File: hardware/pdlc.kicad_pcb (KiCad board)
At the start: 2 copper layers, 56 x 36 mm, 57 parts, among them J1 TBP01R1-508-06BE, Q1 S8550, U1 LM5158, U2 DRV8262DDWR, U3 TLC555IDR

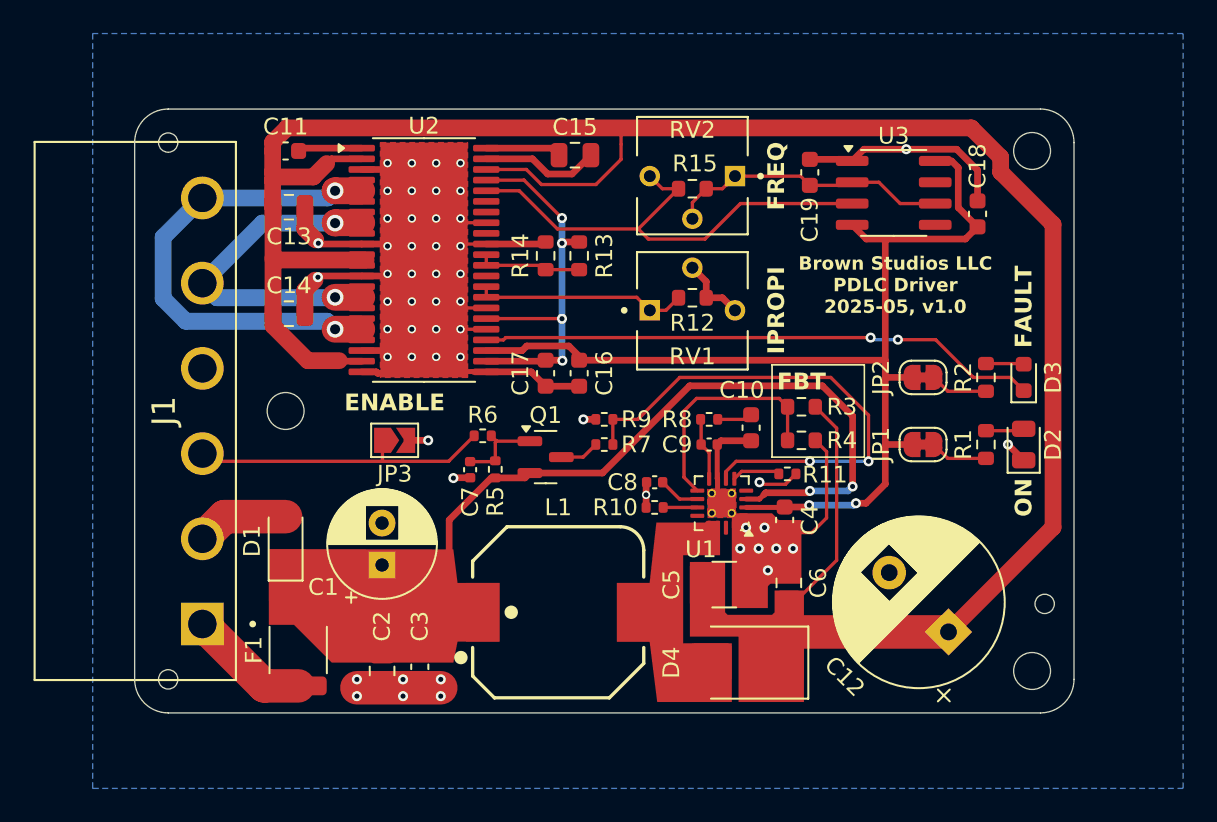
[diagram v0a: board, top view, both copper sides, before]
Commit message: Revised layout using LM5108 and discrete FETs
LM5108 is less expensive but it requires more board area.  In lieu of
active current limiting, we rely on the LM5158 hiccup overload
protection.  The FETs are intentionally oversized to handle large
current pulses when switching the polarity of the capacitive load.

This design is complete and ready for manufacture.
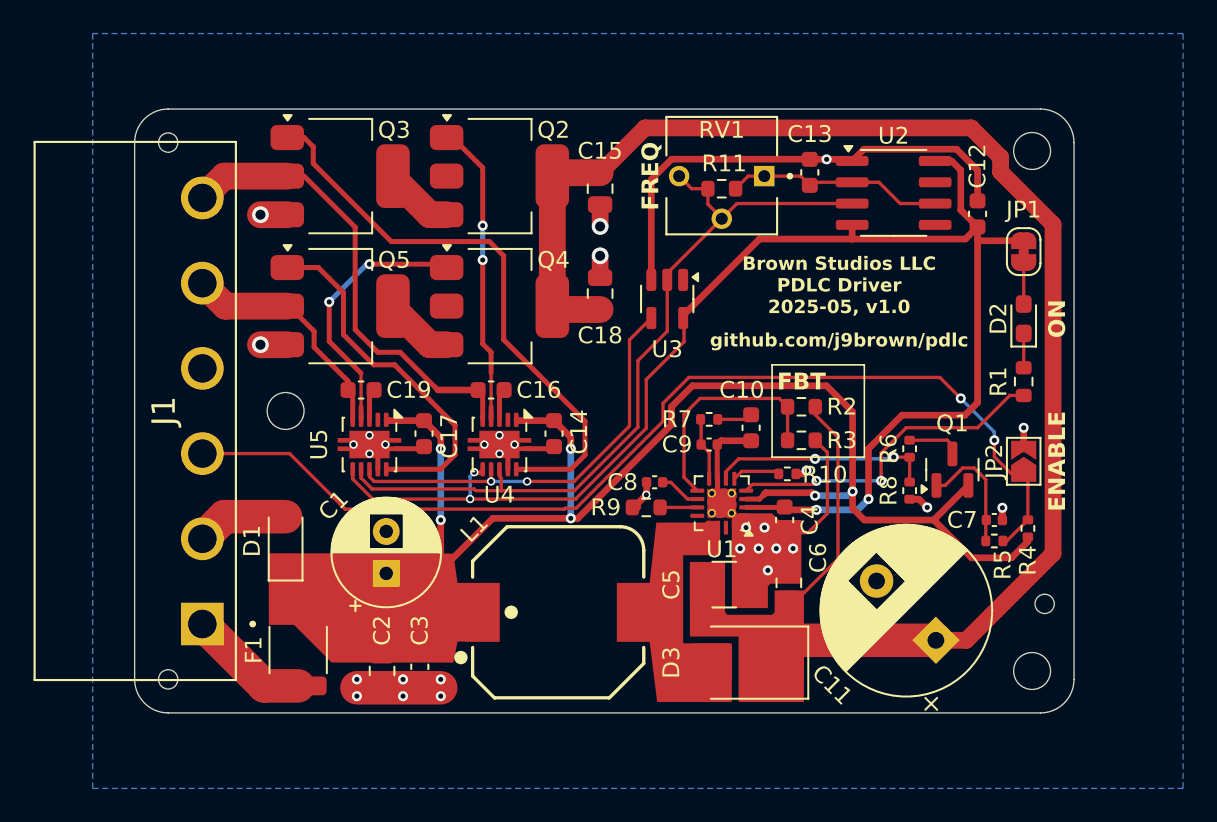
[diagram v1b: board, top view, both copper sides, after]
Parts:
- removed the C12 at (128.5, 113.2)
- removed the C13 at (89.2, 87.8)
- removed the D3 at (133.0, 98.0)
- removed the JP2 at (127.0, 98.0)
- removed R12: 4.7K, Resistor_SMD:R_0603_1608Metric
- removed R13, R14: 100K, Resistor_SMD:R_0603_1608Metric
- removed the R2 at (130.8, 98.0)
- removed the RV1 at (113.2, 94.0)
- removed the U2 at (97.2, 91.0)
- added C18: 100n, Capacitor_SMD:C_0805_2012Metric, F.Cu at (107.8, 93.0)
- added C19: 1u, Capacitor_SMD:C_0603_1608Metric, F.Cu at (93.5, 98.8)
- added Q2: DMN10H120SE, Package_TO_SOT_SMD:SOT-223, F.Cu at (101.8, 86.0)
- added Q3: DMN10H120SE, Package_TO_SOT_SMD:SOT-223, F.Cu at (92.2, 86.0)
- added Q4: DMN10H120SE, Package_TO_SOT_SMD:SOT-223, F.Cu at (101.8, 93.8)
- added Q5: DMN10H120SE, Package_TO_SOT_SMD:SOT-223, F.Cu at (92.2, 93.8)
- added U3: SN74LVC1G14DBV, Package_TO_SOT_SMD:SOT-23-5, F.Cu at (111.8, 93.3)
- added U4: LM5108DRC, Package_SON:VSON-10-1EP_3x3mm_P0.5mm_EP1.65x2.4mm, F.Cu at (101.8, 102.0)
- added U5: LM5108DRC, Package_SON:VSON-10-1EP_3x3mm_P0.5mm_EP1.65x2.4mm, F.Cu at (94.0, 102.0)
- C11: value 1u -> 100u; footprint Capacitor_SMD:C_0603_1608Metric -> Capacitor_THT:CP_Radial_D10.0mm_P5.00mm
- C14: value 100n -> 10u; footprint Capacitor_SMD:C_0805_2012Metric -> Capacitor_SMD:C_0603_1608Metric
- C16: value 100n -> 1u
- C17: value 1u -> 10u
- D2: value KT-0805G -> KT-0603R; footprint LED_SMD:LED_0805_2012Metric -> LED_SMD:LED_0603_1608Metric_Pad1.05x0.95mm_HandSolder
- F1: footprint Fuse:Fuse_1812_4532Metric -> 1812L:1812L
- R5: renamed from R6; value 100K -> 20K
- R9: renamed from R10; value 100K -> 39K; footprint Resistor_SMD:R_0402_1005Metric -> Resistor_SMD:R_0603_1608Metric
- moved C11 48.5 mm to (127.8, 113.7), turned to 135 degrees
- moved JP2 37.5 mm to (133.0, 103.0), turned to 90 degrees
- moved R4 31.9 mm to (133.2, 107.0)
- moved C7 31.4 mm to (131.2, 106.5), turned to 0 degrees
- moved R5 31.1 mm to (131.2, 107.8), turned to 180 degrees
- moved Q1 24.3 mm to (128.8, 103.5), turned to 90 degrees
- moved R8 18.7 mm to (126.2, 104.8), turned to -90 degrees
- moved R6 18.2 mm to (126.2, 102.2), turned to -90 degrees
- moved C14 17.3 mm to (105.0, 101.3), turned to -90 degrees
- moved JP1 13.0 mm to (133.0, 90.5), turned to -90 degrees
- moved NT1 12.3 mm to (112.8, 95.6), turned to -90 degrees
- moved C17 8.09 mm to (97.2, 101.3)
- moved D2 7.50 mm to (133.0, 94.5)
- moved C16 5.34 mm to (101.2, 98.8), turned to 180 degrees
- moved R1 4.37 mm to (133.0, 98.2), turned to -90 degrees
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- renumbered C18 to C12, C19 to C13, D4 to D3, JP3 to JP2, R11 to R10, R15 to R11, R3 to R2, R4 to R3, R5 to R4, R7 to R6, R8 to R7, R9 to R8, RV2 to RV1, U3 to U2
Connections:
- C11 pad 1: Net-(U2-VCP) -> VPDLC
- C11 pad 2: VPDLC -> GND
- C13 pad 1: Net-(U3-THR) -> Net-(U2-THR)
- C14 pad 1: VPDLC -> +12V
- C15 pad 1: Net-(U2-CPH) -> VPDLC
- C15 pad 2: Net-(U2-CPL) -> GND
- C16 pad 1: +5V -> /inverter/half-bridge A/HB
- C16 pad 2: GND -> /OUTA
- C17 pad 1: /inverter/DVDD -> +12V
- D2 pad 1: GND -> Net-(D2-K)
- JP1 pad 2: Net-(JP1-B) -> Net-(D2-A)
- NT1 pad 1: Net-(U2-~{SLEEP}) -> +5V
- NT1 pad 2: VPDLC -> /inverter/half-bridge A/EN
- R1 pad 1: Net-(JP1-B) -> Net-(D2-K)
- R1 pad 2: Net-(D2-A) -> PGOOD
- R11 pad 2: Net-(U3-THR) -> Net-(U2-THR)
- R4 pad 2: Net-(Q1-B) -> /~{EN}
- RV1 pad 1: Net-(U3-THR) -> Net-(U2-THR)
- RV1 pad 2: Net-(U3-THR) -> /inverter/PHASE
- U1 pad 4: unconnected-(U1-PGOOD-Pad4) -> PGOOD
- U2 pad 2: Net-(U3-THR) -> Net-(U2-THR)
- U2 pad 6: Net-(U3-THR) -> Net-(U2-THR)
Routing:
- net /~{EN}: track 17.6 -> 62.0 mm, vias 0 -> 2
- net +12V: track 41.0 -> 76.6 mm, vias 2 -> 6
- net /inverter/half-bridge A/LO: track 0.00 -> 34.7 mm
- net VPDLC: track 128.6 -> 94.2 mm
- net /~{FAULT}: track 33.4 -> 0.00 mm, vias 2 -> 0
- net /inverter/half-bridge A/EN: track 0.00 -> 28.8 mm, vias 0 -> 2
- net /inverter/~{PHASE}: track 0.00 -> 25.1 mm, vias 0 -> 2
- net /inverter/DVDD: track 24.0 -> 0.00 mm, vias 4 -> 0
- net /inverter/half-bridge B/LO: track 0.00 -> 21.6 mm
- net PGOOD: track 0.00 -> 19.9 mm, vias 0 -> 2
- net /inverter/half-bridge A/HO: track 0.00 -> 17.8 mm, vias 0 -> 2
- net /boost/UVLO: track 30.6 -> 13.2 mm
- net /inverter/PHASE: track 29.3 -> 46.6 mm
- net Net-(U3-THR): track 16.7 -> 0.00 mm
- net /inverter/half-bridge B/HO: track 0.00 -> 15.5 mm, vias 0 -> 2
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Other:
- board text added: "${COMMENT1}"
- board text added: "${COMPANY} ${TITLE} ${ISSUE_DATE}, ${REVISION} ${COMMENT1}"
- board text removed: "${COMMENT1} ${COMPANY} ${TITLE} ${ISSUE_DATE}, ${REVISION}"
- board text removed: "FAULT"
- board text removed: "IPROPI"
